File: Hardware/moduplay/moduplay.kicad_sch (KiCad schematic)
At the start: 16 parts, among them J2 -, J3 +, SW1 Left, SW10 Power_Switch, SW11 Buzzer_Switch, SW2 Up, SW3 Right, SW4 Down, SW5 X, SW6 Y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

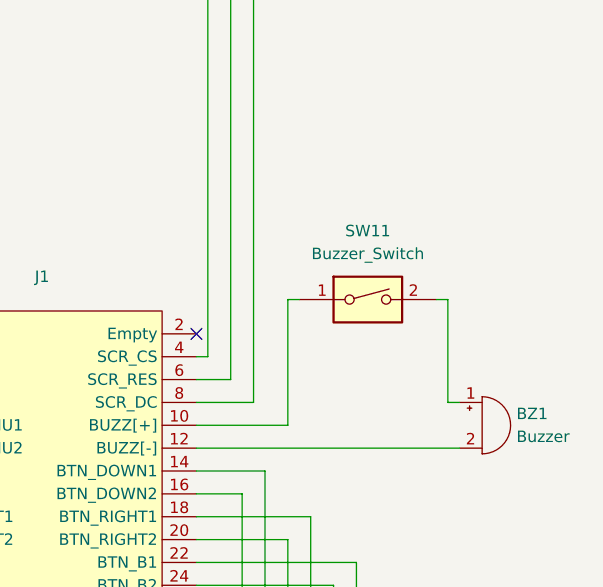
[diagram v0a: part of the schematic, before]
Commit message: Fix buzzer connection
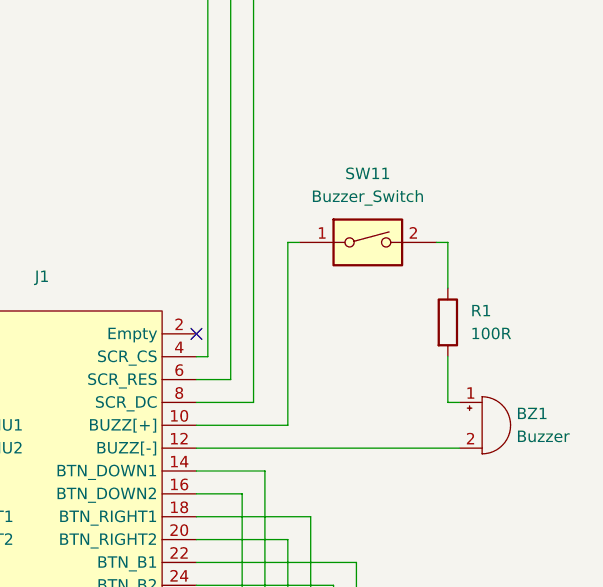
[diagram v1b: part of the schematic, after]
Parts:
- added R1: 100R, Resistor_SMD:R_1206_3216Metric_Pad1.30x1.75mm_HandSolder, symbol Device:R
- BZ1: footprint Buzzer_Beeper:Buzzer_12x9.5RM7.6 -> Buzzer_Beeper:Buzzer_TDK_PS1240P02BT_D12.2mm_H6.5mm
- DS1: footprint local:Screen_Port -> local:Screen_Full
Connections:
- net at BZ1.1 (+): now also R1.2; no longer SW11.2
- new net: R1.1, SW11.2
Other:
- moved on the sheet: SW11
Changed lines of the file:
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@@
 	(wire
 		(pts
-			(xy 251.46 71.12) (xy 252.73 71.12)
+			(xy 251.46 64.77) (xy 252.73 64.77)
 		)
 		(stroke
@@
 	(wire
 		(pts
-			(xy 269.24 71.12) (xy 267.97 71.12)
+			(xy 269.24 64.77) (xy 267.97 64.77)
 		)
 		(stroke
@@
 	(wire
 		(pts
-			(xy 269.24 82.55) (xy 269.24 71.12)
+			(xy 269.24 82.55) (xy 269.24 77.47)
 		)
 		(stroke
@@
 	(wire
 		(pts
+			(xy 269.24 69.85) (xy 269.24 64.77)
+		)
+		(stroke
+			(width 0)
+			(type default)
+		)
+	)
+	(wire
+		(pts
 			(xy 137.16 85.09) (xy 162.56 85.09)
 		)
@@
 	(wire
 		(pts
-			(xy 251.46 71.12) (xy 251.46 85.09)
+			(xy 251.46 64.77) (xy 251.46 85.09)
 		)
 		(stroke
@@
 			)
 		)
-		(property "Footprint" "Buzzer_Beeper:Buzzer_12x9.5RM7.6"
+		(property "Footprint" "Buzzer_Beeper:Buzzer_TDK_PS1240P02BT_D12.2mm_H6.5mm"
 			(at 272.415 82.55 90)
 			(effects
@@
 	(symbol
 		(lib_id "Switch:SW_DIP_x01")
-		(at 260.35 71.12 0)
+		(at 260.35 64.77 0)
 		(unit 1)
 		(exclude_from_sim no)
@@
 		(fields_autoplaced yes)
 		(property "Reference" "SW11"
-			(at 260.35 63.5 0)
+			(at 260.35 57.15 0)
 			(effects
 				(font
@@
 		)
 		(property "Value" "Buzzer_Switch"
-			(at 260.35 66.04 0)
+			(at 260.35 59.69 0)
 			(effects
 				(font
@@
 		)
 		(property "Footprint" "local:Power_Switch"
-			(at 260.35 71.12 0)
+			(at 260.35 64.77 0)
 			(effects
 				(font
@@
 		)
 		(property "Datasheet" "~"
-			(at 260.35 71.12 0)
+			(at 260.35 64.77 0)
 			(effects
 				(font
@@
 		)
 		(property "Description" "1x DIP Switch, Single Pole Single Throw (SPST) switch, small symbol"
-			(at 260.35 71.12 0)
+			(at 260.35 64.77 0)
 			(effects
 				(font
@@
 	)
 	(symbol
+		(lib_id "Device:R")
+		(at 269.24 73.66 0)
+		(unit 1)
+		(exclude_from_sim no)
+		(in_bom yes)
+		(on_board yes)
+		(dnp no)
+		(fields_autoplaced yes)
+		(property "Reference" "R1"
+			(at 271.78 72.3899 0)
+			(effects
+				(font
+					(size 1.27 1.27)
+				)
+				(justify left)
+			)
+		)
+		(property "Value" "100R"
+			(at 271.78 74.9299 0)
+			(effects
+				(font
+					(size 1.27 1.27)
+				)
+				(justify left)
+			)
+		)
+		(property "Footprint" "Resistor_SMD:R_1206_3216Metric_Pad1.30x1.75mm_HandSolder"
+			(at 267.462 73.66 90)
+			(effects
+				(font
+					(size 1.27 1.27)
+				)
+				(hide yes)
+			)
+		)
+		(property "Datasheet" "~"
+			(at 269.24 73.66 0)
+			(effects
+				(font
+					(size 1.27 1.27)
+				)
+				(hide yes)
+			)
+		)
+		(property "Description" "Resistor"
+			(at 269.24 73.66 0)
+			(effects
+				(font
+					(size 1.27 1.27)
+				)
+				(hide yes)
+			)
+		)
+		(pin "2"
+		)
+		(pin "1"
+		)
+		(instances
+			(project ""
+				(path "/a0f040db-288e-40cf-b064-eb69da64d287"
+					(reference "R1")
+					(unit 1)
+				)
+			)
+		)
+	)
+	(symbol
 		(lib_id "Connector_Generic:Conn_01x01")
 		(at 80.01 166.37 180)
@@
 			)
 		)
-		(property "Footprint" "local:Screen_Port"
+		(property "Footprint" "local:Screen_Full"
 			(at 109.22 43.18 0)
 			(effects
